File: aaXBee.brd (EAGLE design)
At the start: 99.1 x 61 mm, 82 parts, among them Q1 IRLML6244TR, SW1 RESET, SW7 SW7, U1 ATmega328P-AU, U2 DS3231, U3 MCP9808, U4 MCP1640D, U5 MCP1640D, Y1 8MHz

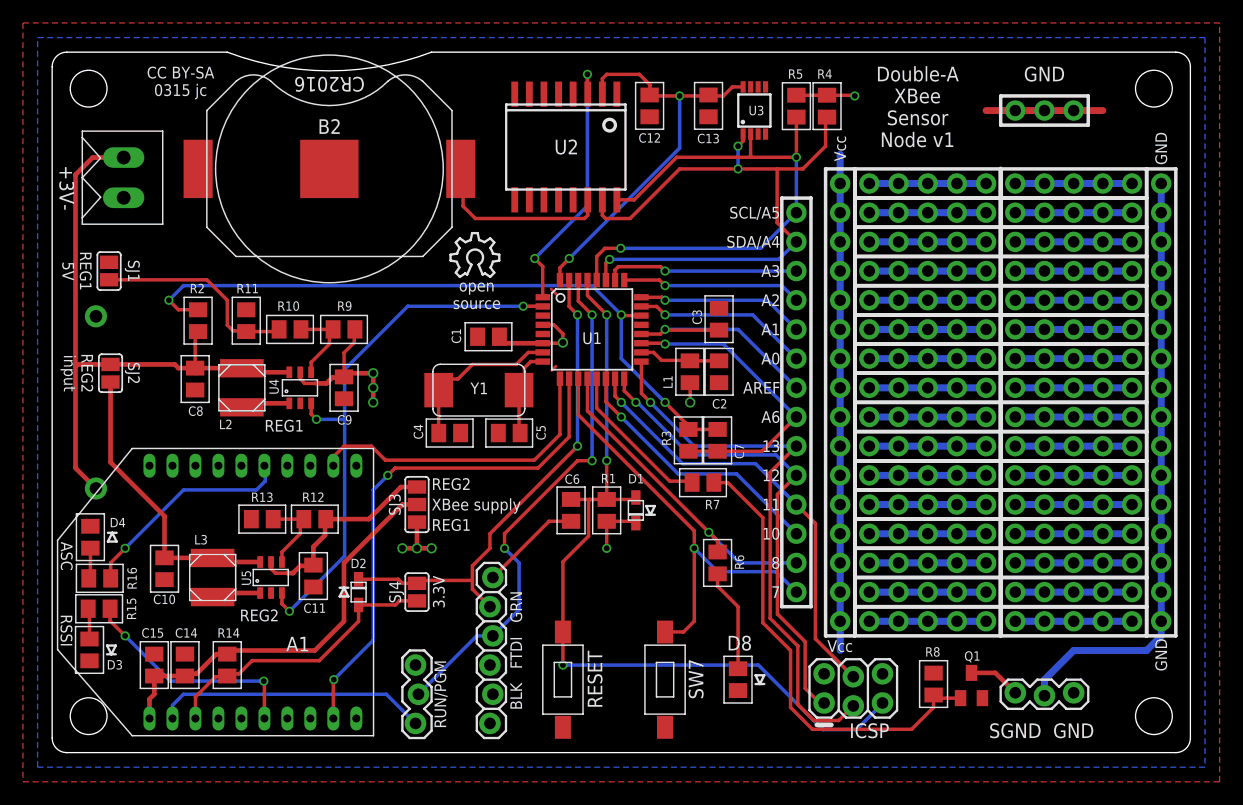
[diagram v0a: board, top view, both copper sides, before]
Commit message: Improved footprint for U3, change Q1 to Si2302CDS, added documentation and photos.
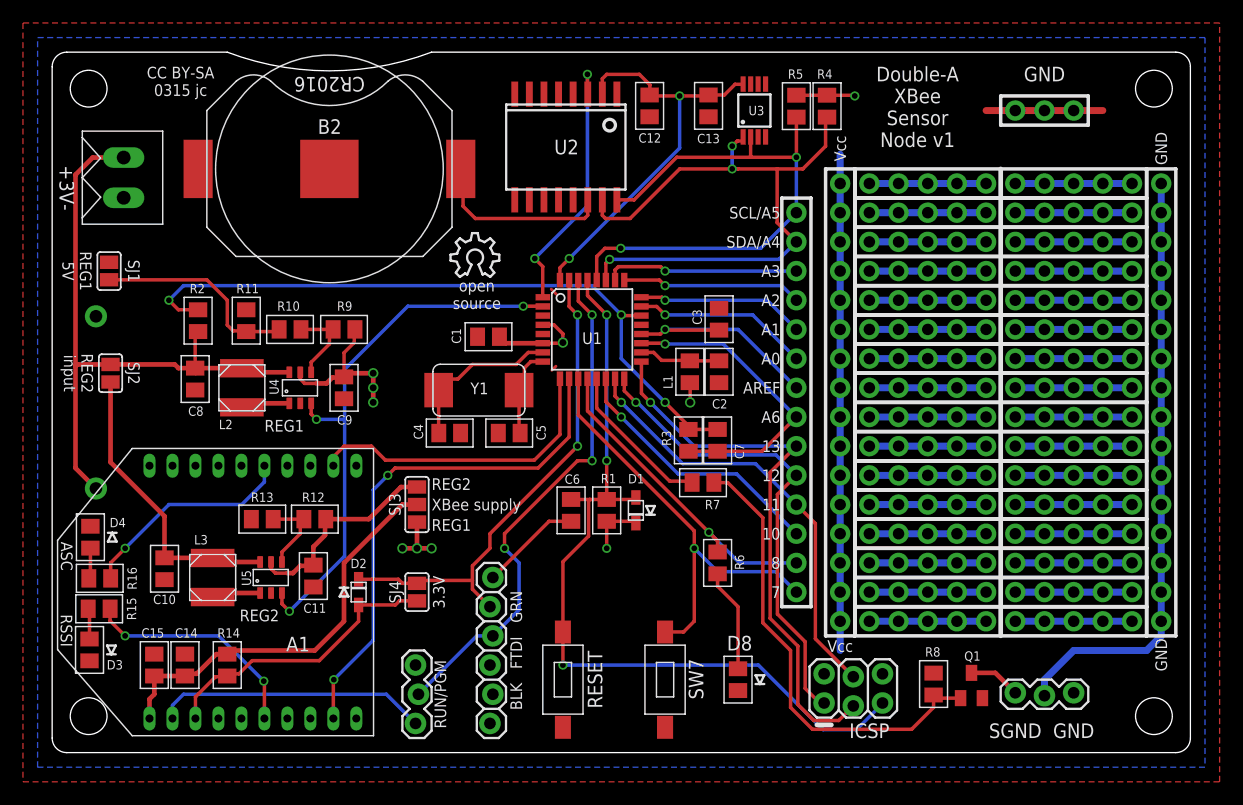
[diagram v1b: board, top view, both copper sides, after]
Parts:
- Q1: value IRLML6244TR -> Si2302CDS
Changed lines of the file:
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@@
 <element name="PR11" library="_jc" package="PROTO-10" value="PROTO-10" x="82.55" y="34.29" smashed="yes"/>
 <element name="PR12" library="_jc" package="PROTO-10" value="PROTO-10" x="82.55" y="46.99" smashed="yes"/>
-<element name="Q1" library="_jc" package="SOT23" value="IRLML6244TR" x="80.01" y="5.842" smashed="yes">
+<element name="Q1" library="_jc" package="SOT23" value="Si2302CDS" x="80.01" y="5.842" smashed="yes">
 <attribute name="NAME" x="79.375" y="8.001" size="0.8128" layer="25" ratio="16"/>
 <attribute name="VALUE" x="78.105" y="2.667" size="0.8128" layer="27" ratio="16"/>
@@
 <wire x1="54.356" y1="51.816" x2="60.833" y2="51.816" width="0.3048" layer="1"/>
 <wire x1="60.833" y1="51.816" x2="64.77" y2="51.816" width="0.3048" layer="1"/>
-<wire x1="60.7874" y1="53.83" x2="60.7874" y2="51.8616" width="0.3048" layer="1"/>
+<wire x1="60.7874" y1="53.58" x2="60.7874" y2="51.8616" width="0.3048" layer="1"/>
 <wire x1="60.7874" y1="51.8616" x2="60.833" y2="51.816" width="0.3048" layer="1"/>
 </signal>
@@
 <wire x1="67.31" y1="52.7812" x2="67.31" y2="55.184" width="0.3048" layer="1"/>
 <wire x1="67.31" y1="55.184" x2="67.437" y2="55.311" width="0.3048" layer="1"/>
-<via x="59.69" y="52.7812" extent="1-16" drill="0.5"/>
-<wire x1="59.7408" y1="50.8508" x2="59.69" y2="50.8" width="0.3048" layer="16"/>
-<via x="59.69" y="50.8" extent="1-16" drill="0.5"/>
-<wire x1="54.61" y1="50.8" x2="59.69" y2="50.8" width="0.3048" layer="1"/>
+<via x="59.182" y="52.7812" extent="1-16" drill="0.5"/>
+<wire x1="54.61" y1="50.8" x2="59.182" y2="50.8" width="0.3048" layer="1"/>
+<wire x1="59.69" y1="50.8" x2="63.0936" y2="50.8" width="0.3048" layer="1"/>
 <wire x1="65.3288" y1="50.8" x2="63.0936" y2="50.8" width="0.3048" layer="1"/>
-<wire x1="63.0936" y1="50.8" x2="59.69" y2="50.8" width="0.3048" layer="1"/>
 <wire x1="63.0936" y1="50.8" x2="63.0936" y2="46.1264" width="0.3048" layer="1"/>
 <wire x1="63.0936" y1="46.1264" x2="64.77" y2="44.45" width="0.3048" layer="1"/>
-<wire x1="60.1374" y1="53.83" x2="60.1374" y2="53.2286" width="0.3048" layer="1"/>
-<wire x1="60.1374" y1="53.2286" x2="59.69" y2="52.7812" width="0.3048" layer="1"/>
-<wire x1="59.69" y1="52.7812" x2="59.69" y2="50.8" width="0.3048" layer="16"/>
+<wire x1="60.1374" y1="53.58" x2="60.1374" y2="53.2286" width="0.3048" layer="1"/>
+<wire x1="60.1374" y1="53.2286" x2="59.6294" y2="53.2286" width="0.3048" layer="1"/>
+<wire x1="59.6294" y1="53.2286" x2="59.182" y2="52.7812" width="0.3048" layer="1"/>
+<wire x1="59.182" y1="52.7812" x2="59.182" y2="50.8" width="0.3048" layer="16"/>
+<via x="59.182" y="50.8" extent="1-16" drill="0.5"/>
+<wire x1="59.182" y1="50.8" x2="59.69" y2="50.8" width="0.3048" layer="1"/>
 </signal>
 <signal name="SCK">
@@
 <contactref element="C13" pad="1"/>
 <contactref element="U1" pad="32"/>
-<wire x1="60.1374" y1="57.93" x2="59.2" y2="57.93" width="0.3048" layer="1"/>
-<wire x1="59.2" y1="57.93" x2="58.42" y2="57.15" width="0.3048" layer="1"/>
-<wire x1="58.42" y1="57.15" x2="57.211" y2="57.15" width="0.3048" layer="1"/>
-<wire x1="57.211" y1="57.15" x2="57.1246" y2="57.2364" width="0.3048" layer="1"/>
 <via x="54.61" y="57.15" extent="1-16" drill="0.5"/>
 <wire x1="54.61" y1="57.15" x2="57.0382" y2="57.15" width="0.3048" layer="1"/>
@@
 <wire x1="45" y1="43" x2="54.61" y2="52.61" width="0.3048" layer="16"/>
 <wire x1="54.61" y1="52.61" x2="54.61" y2="57.15" width="0.3048" layer="16"/>
+<wire x1="57.1246" y1="57.2364" x2="58.5064" y2="57.2364" width="0.3048" layer="1"/>
+<wire x1="58.5064" y1="57.2364" x2="59.436" y2="58.166" width="0.3048" layer="1"/>
+<wire x1="59.436" y1="58.166" x2="60.1234" y2="58.166" width="0.3048" layer="1"/>
+<wire x1="60.1234" y1="58.166" x2="60.1374" y2="58.18" width="0.3048" layer="1"/>
 </signal>
 <signal name="SPWR">
@@
 <wire x1="5.0902" y1="16.5202" x2="6.35" y2="17.78" width="0.3048" layer="1"/>
 <via x="6.35" y="17.78" extent="1-16" drill="0.5"/>
-<wire x1="6.35" y1="17.78" x2="11.43" y2="22.86" width="0.3048" layer="16"/>
-<wire x1="11.43" y1="22.86" x2="17.78" y2="22.86" width="0.3048" layer="16"/>
-<wire x1="17.78" y1="22.86" x2="18.542" y2="23.622" width="0.3048" layer="16"/>
-<wire x1="18.542" y1="23.622" x2="18.542" y2="24.898" width="0.3048" layer="16"/>
-<wire x1="18.542" y1="24.898" x2="18.47" y2="24.97" width="0.3048" layer="16"/>
+<wire x1="6.35" y1="17.78" x2="10.16" y2="21.59" width="0.3048" layer="16"/>
+<wire x1="10.16" y1="21.59" x2="16.51" y2="21.59" width="0.3048" layer="16"/>
+<wire x1="16.51" y1="21.59" x2="18.47" y2="23.55" width="0.3048" layer="16"/>
+<wire x1="18.47" y1="23.55" x2="18.47" y2="24.97" width="0.3048" layer="16"/>
 </signal>
 <signal name="RSSI">
@@
 <wire x1="5.0394" y1="11.4706" x2="6.35" y2="10.16" width="0.3048" layer="1"/>
 <via x="6.35" y="10.16" extent="1-16" drill="0.5"/>
-<wire x1="6.35" y1="10.16" x2="10.287" y2="6.223" width="0.3048" layer="16"/>
-<wire x1="10.287" y1="6.223" x2="18.415" y2="6.223" width="0.3048" layer="16"/>
 <via x="18.415" y="6.223" extent="1-16" drill="0.5"/>
 <wire x1="18.415" y1="6.223" x2="18.47" y2="6.168" width="0.3048" layer="1"/>
 <wire x1="18.47" y1="6.168" x2="18.47" y2="2.97" width="0.3048" layer="1"/>
+<wire x1="6.35" y1="10.16" x2="14.478" y2="10.16" width="0.3048" layer="16"/>
+<wire x1="14.478" y1="10.16" x2="18.415" y2="6.223" width="0.3048" layer="16"/>
 </signal>
 <signal name="AREF">

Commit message: Change Q1 to IRLML6344TRPBF.
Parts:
- Q1: value Si2302CDS -> IRLML6344TRPBF
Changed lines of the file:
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@@
 <element name="PR11" library="_jc" package="PROTO-10" value="PROTO-10" x="82.55" y="34.29" smashed="yes"/>
 <element name="PR12" library="_jc" package="PROTO-10" value="PROTO-10" x="82.55" y="46.99" smashed="yes"/>
-<element name="Q1" library="_jc" package="SOT23" value="Si2302CDS" x="80.01" y="5.842" smashed="yes">
+<element name="Q1" library="_jc" package="SOT23" value="IRLML6344TRPBF" x="80.01" y="5.842" smashed="yes">
 <attribute name="NAME" x="79.375" y="8.001" size="0.8128" layer="25" ratio="16"/>
 <attribute name="VALUE" x="78.105" y="2.667" size="0.8128" layer="27" ratio="16"/>
